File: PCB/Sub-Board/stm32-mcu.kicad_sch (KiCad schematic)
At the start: 42 parts, among them J2 Conn_01x04_Pin, U2 74HC165, U3 STM32F401VETx, U4 74HC165, U5 74HC165, U6 74HC165, U7 74HC165, Y1 26 MHz

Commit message: Sub Board PCB: Routing (wip)
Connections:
- net GNDD is gone; now on net GND: C14.2, C17.2, C21.2, C24.2, C3.2, C4.2, C5.2, C6.2, R24.1, U2.10 (DS), U2.15 (~{CE}), U4.15 (~{CE}), U5.15 (~{CE}), U6.15 (~{CE}), U7.15 (~{CE})
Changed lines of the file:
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@@
 			)
 		)
-		(property "Value" "GNDD"
+		(property "Value" "GND"
 			(at 378.46 206.0631 0)
 			(effects
@@
 			)
 		)
-		(property "Value" "GNDD"
+		(property "Value" "GND"
 			(at 205.74 96.8431 0)
 			(effects
@@
 			)
 		)
-		(property "Value" "GNDD"
+		(property "Value" "GND"
 			(at 276.86 96.8431 0)
 			(effects
@@
 			)
 		)
-		(property "Value" "GNDD"
+		(property "Value" "GND"
 			(at 63.5 96.8431 0)
 			(effects
@@
 			)
 		)
-		(property "Value" "GNDD"
+		(property "Value" "GND"
 			(at 341.63 206.0631 0)
 			(effects
@@
 			)
 		)
-		(property "Value" "GNDD"
+		(property "Value" "GND"
 			(at 360.68 193.3631 0)
 			(effects
@@
 			)
 		)
-		(property "Value" "GNDD"
+		(property "Value" "GND"
 			(at 134.62 96.8431 0)
 			(effects
@@
 			)
 		)
-		(property "Value" "GNDD"
+		(property "Value" "GND"
 			(at 347.98 96.8431 0)
 			(effects

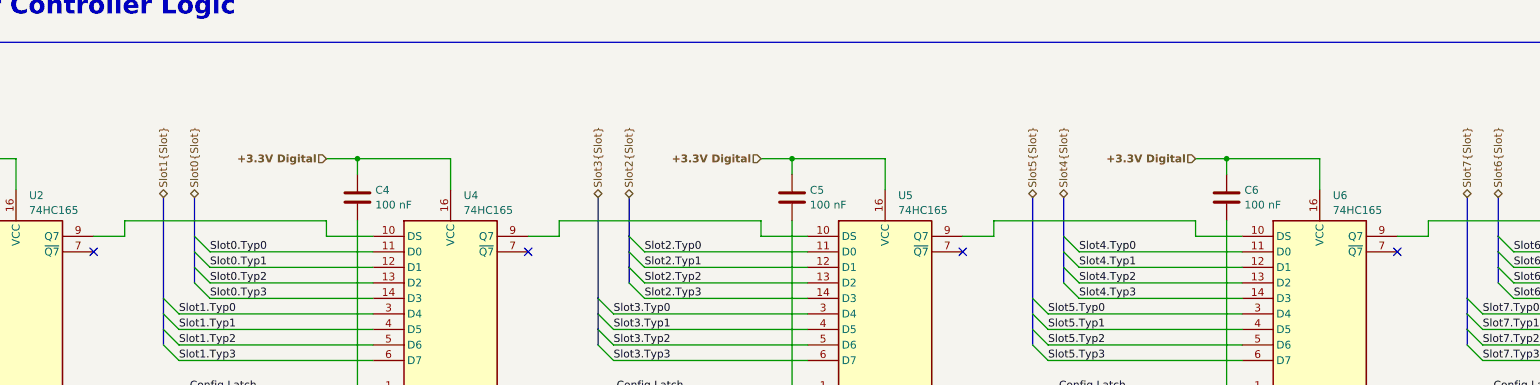
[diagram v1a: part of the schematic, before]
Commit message: Sub Board PCB: More routing
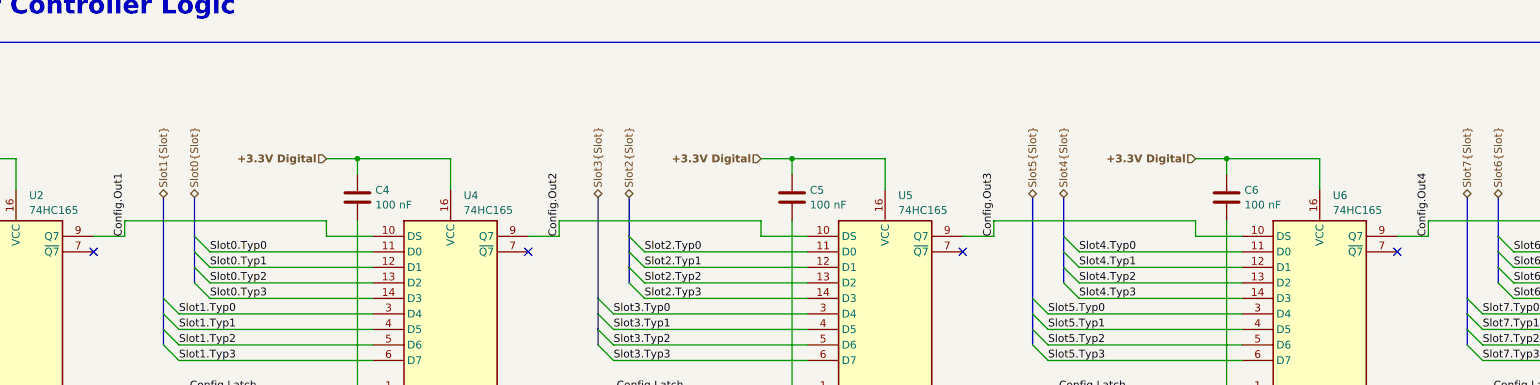
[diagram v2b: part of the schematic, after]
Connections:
- net Config.Out1: now reaches U2.9 (Q7), U4.10 (DS)
- net Config.Out2: now reaches U4.9 (Q7), U5.10 (DS)
- net Config.Out3: now reaches U5.9 (Q7), U6.10 (DS)
- net Config.Out4: now reaches U6.9 (Q7), U7.10 (DS)
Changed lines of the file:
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@@
+		)
+	)
+	(label "Config.Out4"
+		(at 309.88 57.15 90)
+		(effects
+			(font
+				(size 1.27 1.27)
+			)
+			(justify left bottom)
+		)
+	)
+	(label "Config.Out3"
+		(at 238.76 57.15 90)
+		(effects
+			(font
+				(size 1.27 1.27)
+			)
+			(justify left bottom)
+		)
+	)
+	(label "Config.Out1"
+		(at 96.52 57.15 90)
+		(effects
+			(font
+				(size 1.27 1.27)
+			)
+			(justify left bottom)
+		)
+	)
+	(label "Config.Out2"
+		(at 167.64 57.15 90)
+		(effects
+			(font
+				(size 1.27 1.27)
+			)
+			(justify left bottom)
 		)
 	)

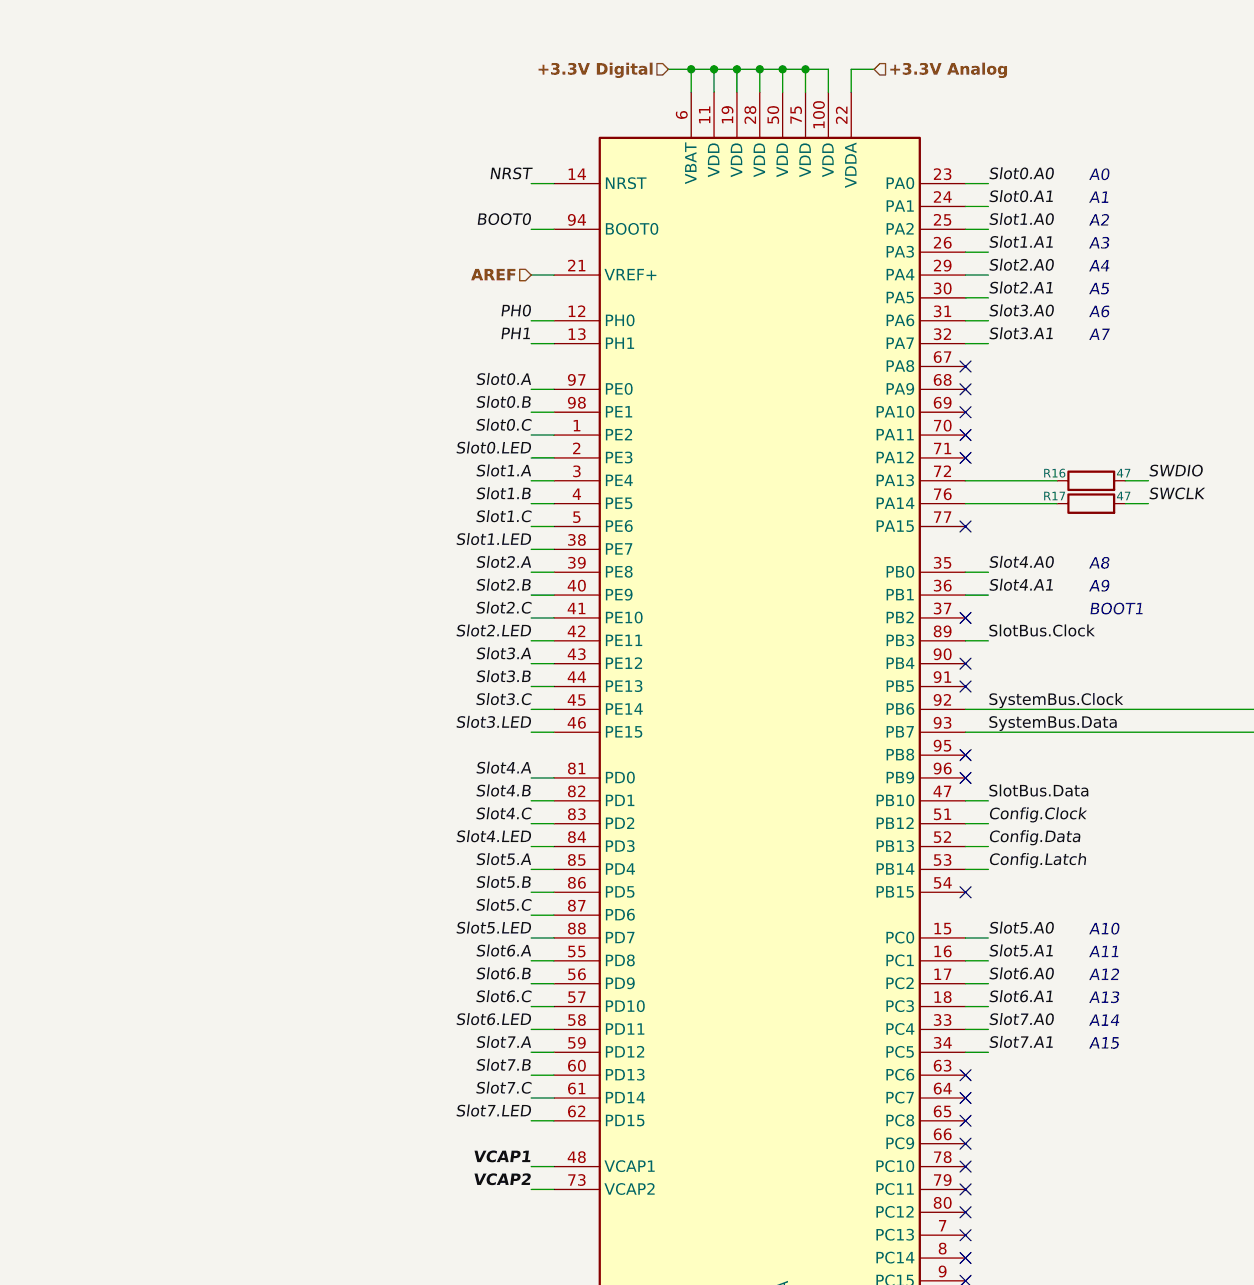
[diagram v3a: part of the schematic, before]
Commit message: Sub Board PCB: Slot routing (wip)
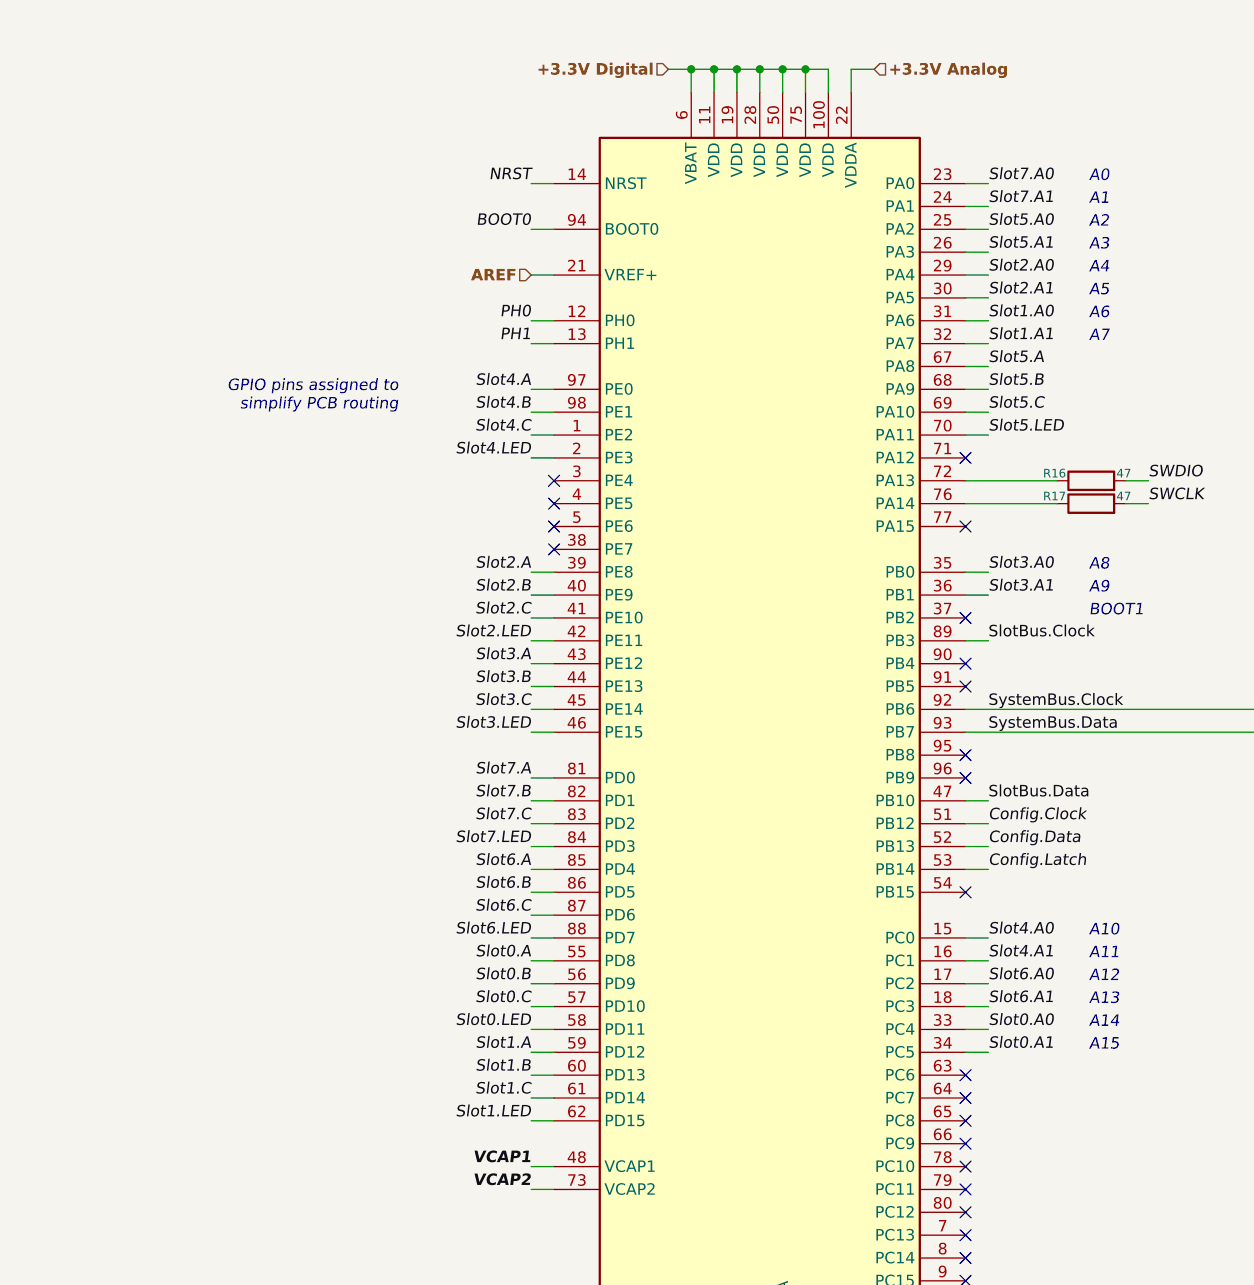
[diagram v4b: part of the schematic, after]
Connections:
- net Slot0.A: now also U3.55 (PD8); no longer U3.97 (PE0)
- net Slot0.A0: now also U3.33 (PC4); no longer U3.23 (PA0)
- net Slot0.A1: now also U3.34 (PC5); no longer U3.24 (PA1)
- net Slot0.B: now also U3.56 (PD9); no longer U3.98 (PE1)
- net Slot0.C: now also U3.57 (PD10); no longer U3.1 (PE2)
- net Slot0.LED: now also U3.58 (PD11); no longer U3.2 (PE3)
- net Slot1.A: now also U3.59 (PD12); no longer U3.3 (PE4)
- net Slot1.A0: now also U3.31 (PA6); no longer U3.25 (PA2)
- net Slot1.A1: now also U3.32 (PA7); no longer U3.26 (PA3)
- net Slot1.B: now also U3.60 (PD13); no longer U3.4 (PE5)
- net Slot1.C: now also U3.61 (PD14); no longer U3.5 (PE6)
- net Slot1.LED: now also U3.62 (PD15); no longer U3.38 (PE7)
- net Slot3.A0: now also U3.35 (PB0); no longer U3.31 (PA6)
- net Slot3.A1: now also U3.36 (PB1); no longer U3.32 (PA7)
- net Slot4.A: now also U3.97 (PE0); no longer U3.81 (PD0)
- net Slot4.A0: now also U3.15 (PC0); no longer U3.35 (PB0)
- net Slot4.A1: now also U3.16 (PC1); no longer U3.36 (PB1)
- net Slot4.B: now also U3.98 (PE1); no longer U3.82 (PD1)
- net Slot4.C: now also U3.1 (PE2); no longer U3.83 (PD2)
- net Slot4.LED: now also U3.2 (PE3); no longer U3.84 (PD3)
- net Slot5.A: now also U3.67 (PA8); no longer U3.85 (PD4)
- net Slot5.A0: now also U3.25 (PA2); no longer U3.15 (PC0)
- net Slot5.A1: now also U3.26 (PA3); no longer U3.16 (PC1)
- net Slot5.B: now also U3.68 (PA9); no longer U3.86 (PD5)
- net Slot5.C: now also U3.69 (PA10); no longer U3.87 (PD6)
- net Slot5.LED: now also U3.70 (PA11); no longer U3.88 (PD7)
- net Slot6.A: now also U3.85 (PD4); no longer U3.55 (PD8)
- net Slot6.B: now also U3.86 (PD5); no longer U3.56 (PD9)
- net Slot6.C: now also U3.87 (PD6); no longer U3.57 (PD10)
- net Slot6.LED: now also U3.88 (PD7); no longer U3.58 (PD11)
- net Slot7.A: now also U3.81 (PD0); no longer U3.59 (PD12)
- net Slot7.A0: now also U3.23 (PA0); no longer U3.33 (PC4)
- net Slot7.A1: now also U3.24 (PA1); no longer U3.34 (PC5)
- net Slot7.B: now also U3.82 (PD1); no longer U3.60 (PD13)
- net Slot7.C: now also U3.83 (PD2); no longer U3.61 (PD14)
- net Slot7.LED: now also U3.84 (PD3); no longer U3.62 (PD15)
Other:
- note added: "GPIO pins assigned to simplify PCB routing"
